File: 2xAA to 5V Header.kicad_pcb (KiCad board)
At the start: 2 copper layers, 30 x 14 mm, 9 parts, among them SW1 SPDT, U1 LTC3426

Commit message: Pin header and corners
Added a two pin header for the output to make attaching leads easier and
cleaned up any 90 degree corners in fills.
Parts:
- added P1: CONN_01X02, Pin_Headers:Pin_Header_Angled_1x02, F.Cu at (176.7, 105.0)
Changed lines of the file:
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@@
 (kicad_pcb (version 4) (host pcbnew 4.0.2-stable)
   (general
-    (links 16)
+    (links 18)
     (no_connects 0)
-    (area 149.924999 95.924999 180.075001 110.075001)
+    (area 147.021999 93.871 190.909334 112.481)
     (thickness 1.6)
     (drawings 17)
     (tracks 76)
     (zones 0)
-    (modules 9)
+    (modules 10)
     (nets 8)
   )
   (page A4)
   (layers
-    (0 F.Cu signal)
+    (0 F.Cu signal hide)
     (31 B.Cu signal)
     (32 B.Adhes user)
@@
     (user_trace_width 0.508)
     (trace_clearance 0.2)
-    (zone_clearance 0.2032)
+    (zone_clearance 0.02032)
     (zone_45_only yes)
     (trace_min 0.1524)
@@
     (add_net /Vout)
   )
+  (module Pin_Headers:Pin_Header_Angled_1x02 (layer F.Cu)
+    (at 176.657 105.029)
+    (descr "Through hole pin header")
+    (tags "pin header")
+    (fp_text reference P1 (at 0 -5.1) (layer F.SilkS)
+      (effects (font (size 1 1) (thickness 0.15)))
+    )
+    (fp_text value CONN_01X02 (at 9.144 -3.556) (layer F.Fab) hide
+      (effects (font (size 1 1) (thickness 0.15)))
+    )
+    (fp_line (start -1.5 -1.75) (end -1.5 4.3) (layer F.CrtYd) (width 0.05))
+    (fp_line (start 10.65 -1.75) (end 10.65 4.3) (layer F.CrtYd) (width 0.05))
+    (fp_line (start -1.5 -1.75) (end 10.65 -1.75) (layer F.CrtYd) (width 0.05))
+    (fp_line (start -1.5 4.3) (end 10.65 4.3) (layer F.CrtYd) (width 0.05))
+    (fp_line (start -1.3 -1.55) (end -1.3 0) (layer F.SilkS) (width 0.15))
+    (fp_line (start 0 -1.55) (end -1.3 -1.55) (layer F.SilkS) (width 0.15))
+    (fp_line (start 4.191 -0.127) (end 10.033 -0.127) (layer F.SilkS) (width 0.15))
+    (fp_line (start 10.033 -0.127) (end 10.033 0.127) (layer F.SilkS) (width 0.15))
+    (fp_line (start 10.033 0.127) (end 4.191 0.127) (layer F.SilkS) (width 0.15))
+    (fp_line (start 4.191 0.127) (end 4.191 0) (layer F.SilkS) (width 0.15))
+    (fp_line (start 4.191 0) (end 10.033 0) (layer F.SilkS) (width 0.15))
+    (fp_line (start 1.524 -0.254) (end 1.143 -0.254) (layer F.SilkS) (width 0.15))
+    (fp_line (start 1.524 0.254) (end 1.143 0.254) (layer F.SilkS) (width 0.15))
+    (fp_line (start 1.524 2.286) (end 1.143 2.286) (layer F.SilkS) (width 0.15))
+    (fp_line (start 1.524 2.794) (end 1.143 2.794) (layer F.SilkS) (width 0.15))
+    (fp_line (start 1.524 -1.27) (end 4.064 -1.27) (layer F.SilkS) (width 0.15))
+    (fp_line (start 1.524 1.27) (end 4.064 1.27) (layer F.SilkS) (width 0.15))
+    (fp_line (start 1.524 1.27) (end 1.524 3.81) (layer F.SilkS) (width 0.15))
+    (fp_line (start 1.524 3.81) (end 4.064 3.81) (layer F.SilkS) (width 0.15))
+    (fp_line (start 4.064 2.286) (end 10.16 2.286) (layer F.SilkS) (width 0.15))
+    (fp_line (start 10.16 2.286) (end 10.16 2.794) (layer F.SilkS) (width 0.15))
+    (fp_line (start 10.16 2.794) (end 4.064 2.794) (layer F.SilkS) (width 0.15))
+    (fp_line (start 4.064 3.81) (end 4.064 1.27) (layer F.SilkS) (width 0.15))
+    (fp_line (start 4.064 1.27) (end 4.064 -1.27) (layer F.SilkS) (width 0.15))
+    (fp_line (start 10.16 0.254) (end 4.064 0.254) (layer F.SilkS) (width 0.15))
+    (fp_line (start 10.16 -0.254) (end 10.16 0.254) (layer F.SilkS) (width 0.15))
+    (fp_line (start 4.064 -0.254) (end 10.16 -0.254) (layer F.SilkS) (width 0.15))
+    (fp_line (start 1.524 1.27) (end 4.064 1.27) (layer F.SilkS) (width 0.15))
+    (fp_line (start 1.524 -1.27) (end 1.524 1.27) (layer F.SilkS) (width 0.15))
+    (pad 1 thru_hole rect (at 0 0) (size 2.032 2.032) (drill 1.016) (layers *.Cu *.Mask F.SilkS)
+      (net 3 /Vout))
+    (pad 2 thru_hole oval (at 0 2.54) (size 2.032 2.032) (drill 1.016) (layers *.Cu *.Mask F.SilkS)
+      (net 1 GND))
+    (model Pin_Headers.3dshapes/Pin_Header_Angled_1x02.wrl
+      (at (xyz 0 -0.05 0))
+      (scale (xyz 1 1 1))
+      (rotate (xyz 0 0 90))
+    )
+  )
   (module .pretty:JS102011SAQN (layer F.Cu)
     (at 153.797 105.537 270)
@@
     )
   )
-  (gr_text - (at 178.816 107.95) (layer F.SilkS)
+  (gr_text - (at 178.816 109.347) (layer F.SilkS)
     (effects (font (size 1.5 1.5) (thickness 0.3)))
   )
-  (gr_text + (at 178.816 104.648) (layer F.SilkS)
+  (gr_text + (at 178.816 102.235) (layer F.SilkS)
     (effects (font (size 1.5 1.5) (thickness 0.3)))
   )
-  (gr_text "OUT\n" (at 177.292 102.108) (layer F.SilkS)
+  (gr_text "OUT\n" (at 172.72 102.997) (layer F.SilkS)
     (effects (font (size 1.5 1.5) (thickness 0.3)))
   )
@@
   (gr_line (start 162 110) (end 162 105) (angle 90) (layer Edge.Cuts) (width 0.15))
   (gr_line (start 150 110) (end 162 110) (angle 90) (layer Edge.Cuts) (width 0.15))
+  (segment (start 174.812 107.6325) (end 176.5935 107.6325) (width 0.5) (layer B.Cu) (net 1))
+  (segment (start 176.5935 107.6325) (end 176.657 107.569) (width 0.5) (layer B.Cu) (net 1))
   (segment (start 155.714 108.204) (end 157.48 108.204) (width 0.5) (layer F.Cu) (net 1))
   (via (at 155.714 108.204) (size 0.6) (drill 0.4) (layers F.Cu B.Cu) (net 1))
@@
   (segment (start 153.797 108.037) (end 155.547 108.037) (width 0.5) (layer F.Cu) (net 1))
   (via (at 174.812 107.6325) (size 0.6) (drill 0.4) (layers F.Cu B.Cu) (net 1))
-  (segment (start 174.812 107.6325) (end 175.3835 108.204) (width 0.5) (layer F.Cu) (net 1))
   (segment (start 173.562 107.6325) (end 174.812 107.6325) (width 0.5) (layer F.Cu) (net 1))
-  (segment (start 175.3835 108.204) (end 176.276 108.204) (width 0.5) (layer F.Cu) (net 1))
   (segment (start 171.4935 99.822) (end 171.4935 104.314) (width 0.5) (layer B.Cu) (net 1))
   (segment (start 171.4935 104.314) (end 174.812 107.6325) (width 0.5) (layer B.Cu) (net 1))
@@
     (polygon
       (pts
-        (xy 162.814 99.822) (xy 164.084 99.822) (xy 169.418 99.822) (xy 169.7228 100.076) (xy 169.7228 101.4476)
-        (xy 168.0972 101.4476) (xy 161.4932 101.4476) (xy 159.258 103.632) (xy 156.21 103.632) (xy 154.686 102.108)
-        (xy 154.686 98.044) (xy 160.02 98.044) (xy 160.02 99.822) (xy 161.417 99.822)
-      )
-    )
-  )
-  (zone (net 1) (net_name GND) (layer F.Cu) (hatch edge 0.508)
-    (connect_pads yes (clearance 0.02032))
-    (min_thickness 0.0254)
-    (fill yes (arc_segments 16) (thermal_gap 0.508) (thermal_bridge_width 0.508))
-    (polygon
-      (pts
-        (xy 175.26 109.474) (xy 177.8 109.474) (xy 177.8 106.934) (xy 175.26 106.934)
+        (xy 159.893 99.822) (xy 169.418 99.822) (xy 169.7228 100.076) (xy 169.7228 101.4476) (xy 161.4932 101.4476)
+        (xy 159.258 103.632) (xy 156.21 103.632) (xy 154.686 102.108) (xy 154.686 98.044) (xy 159.512 98.044)
+        (xy 159.512 98.298) (xy 159.766 98.552) (xy 159.766 99.695) (xy 159.893 99.822)
       )
     )
@@
     (polygon
       (pts
-        (xy 170.5356 98.0948) (xy 170.5356 101.9048) (xy 170.942 102.362) (xy 177.8 102.362) (xy 177.8 106.172)
         (xy 172.466 106.172) (xy 171.958 105.918) (xy 171.958 104.14) (xy 169.926 103.378) (xy 164.7952 103.378)
         (xy 164.7952 101.7016) (xy 170.0276 101.7016) (xy 170.0276 100.0252) (xy 169.5196 99.568) (xy 167.64 99.568)
         (xy 167.132 99.314) (xy 164.338 99.314) (xy 164.338 96.52) (xy 168.91 96.52) (xy 170.434 98.044)
+        (xy 170.5356 98.0948) (xy 170.5356 101.9048) (xy 170.942 102.362) (xy 177.165 102.362) (xy 177.8 102.997)
+        (xy 177.8 106.172) (xy 172.466 106.172)
       )
     )
@@
     (polygon
       (pts
-        (xy 168.402 109.474) (xy 168.402 104.648) (xy 161.544 104.648) (xy 161.544 109.474) (xy 151.892 109.474)
-        (xy 151.892 101.6) (xy 155.702 96.52) (xy 174.244 96.52) (xy 179.578 101.854) (xy 179.578 109.474)
+        (xy 179.578 101.854) (xy 179.578 108.966) (xy 179.07 109.474) (xy 168.91 109.474) (xy 168.402 108.966)
+        (xy 168.402 104.902) (xy 168.148 104.648) (xy 161.798 104.648) (xy 161.544 104.902) (xy 161.544 108.966)
+        (xy 161.036 109.474) (xy 152.4 109.474) (xy 151.892 108.966) (xy 151.892 101.6) (xy 155.702 96.52)
+        (xy 174.244 96.52) (xy 179.578 101.854)
       )
     )
-  )
-  (zone (net 0) (net_name "") (layer F.Mask) (hatch edge 0.508)
-    (connect_pads yes (clearance 0.02032))
-    (min_thickness 0.0254)
-    (fill yes (arc_segments 16) (thermal_gap 0.508) (thermal_bridge_width 0.508))
-    (polygon
-      (pts
-        (xy 177.8 106.934) (xy 175.26 106.934) (xy 175.26 109.474) (xy 177.8 109.474)
-      )
-    )
-  )
-  (zone (net 0) (net_name "") (layer F.Mask) (hatch edge 0.508)
-    (connect_pads yes (clearance 0.02032))
-    (min_thickness 0.0254)
-    (fill yes (arc_segments 16) (thermal_gap 0.508) (thermal_bridge_width 0.508))
-    (polygon
-      (pts
-        (xy 177.8 106.172) (xy 175.26 106.172) (xy 175.26 103.632) (xy 177.8 103.632)
-      )
-    )

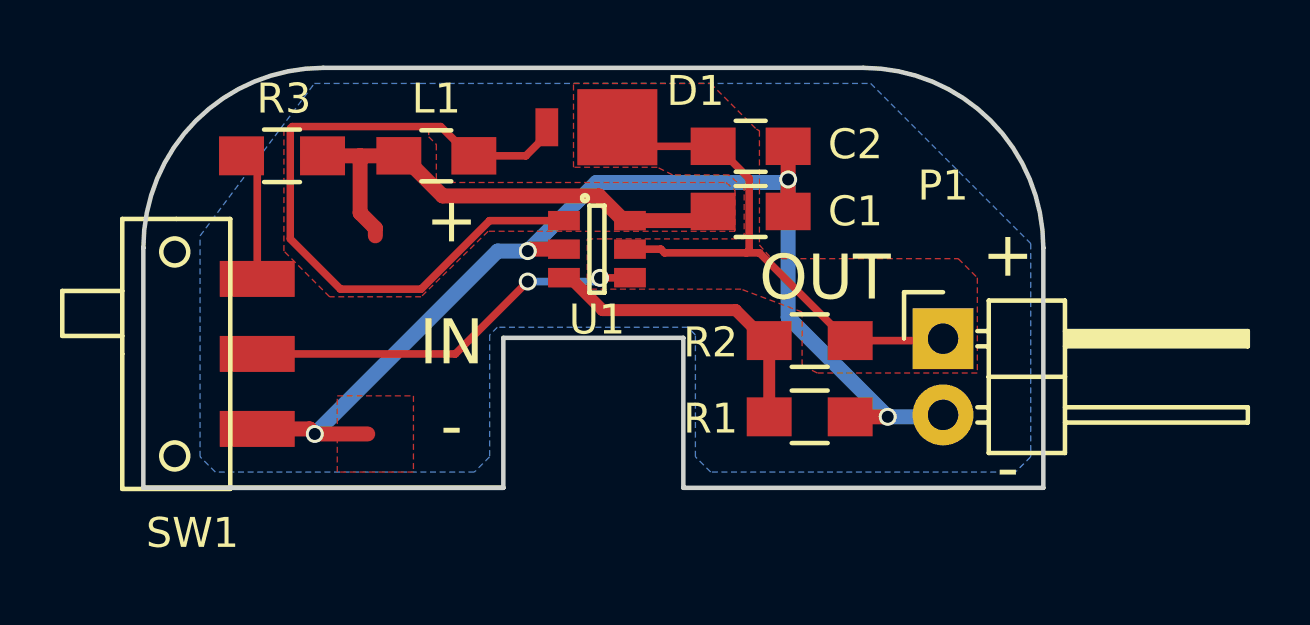
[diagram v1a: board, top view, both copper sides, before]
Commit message: Redo of GND copper fill
Reworked the GND copper fills to cover better and use thermal reliefs.
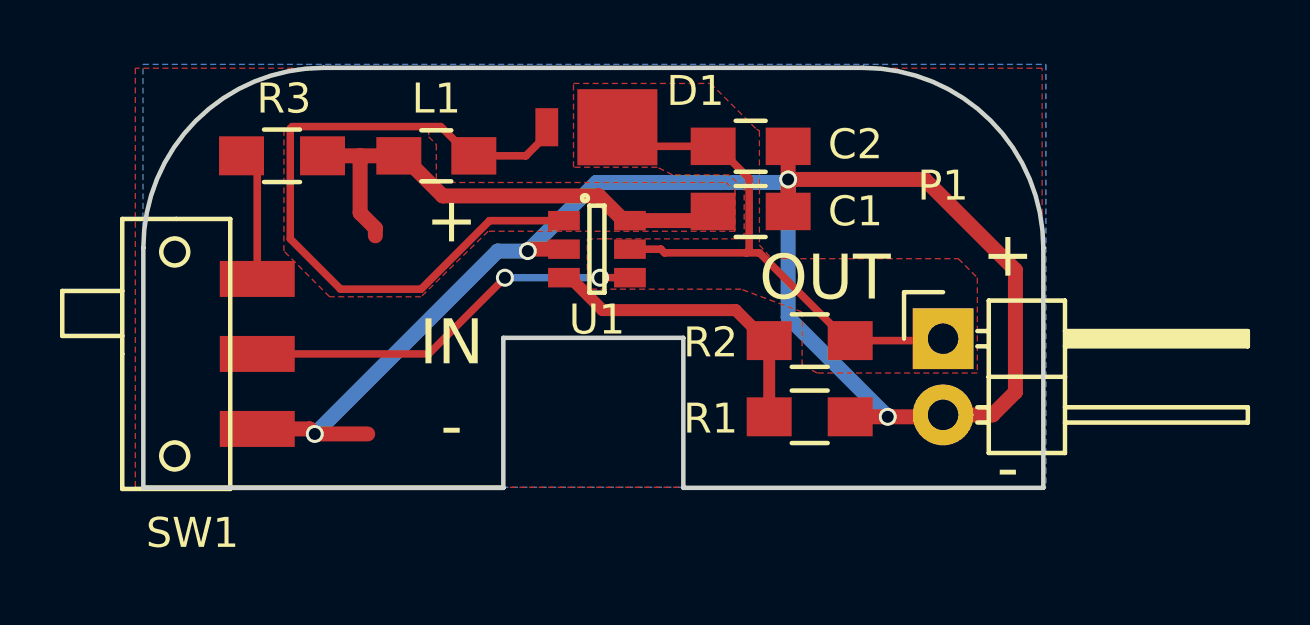
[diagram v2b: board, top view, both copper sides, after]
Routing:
- net GND: track 39.7 -> 55.4 mm
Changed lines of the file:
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@@
     (thickness 1.6)
     (drawings 17)
-    (tracks 76)
+    (tracks 82)
     (zones 0)
     (modules 10)
@@
   (page A4)
   (layers
-    (0 F.Cu signal hide)
+    (0 F.Cu signal)
     (31 B.Cu signal)
     (32 B.Adhes user)
@@
     (user_trace_width 0.508)
     (trace_clearance 0.2)
-    (zone_clearance 0.02032)
+    (zone_clearance 0.1524)
     (zone_45_only yes)
     (trace_min 0.1524)
@@
   (gr_line (start 162 110) (end 162 105) (angle 90) (layer Edge.Cuts) (width 0.15))
   (gr_line (start 150 110) (end 162 110) (angle 90) (layer Edge.Cuts) (width 0.15))
-  (segment (start 174.812 107.6325) (end 176.5935 107.6325) (width 0.5) (layer B.Cu) (net 1))
+  (segment (start 171.4935 99.7204) (end 176.0474 99.7204) (width 0.5) (layer F.Cu) (net 1))
+  (via (at 171.4935 99.7204) (size 0.6) (drill 0.4) (layers F.Cu B.Cu) (net 1))
+  (segment (start 178.308 107.569) (end 176.657 107.569) (width 0.5) (layer F.Cu) (net 1))
+  (segment (start 179.07 106.807) (end 178.308 107.569) (width 0.5) (layer F.Cu) (net 1))
+  (segment (start 179.07 102.743) (end 179.07 106.807) (width 0.5) (layer F.Cu) (net 1))
+  (segment (start 176.0474 99.7204) (end 179.07 102.743) (width 0.5) (layer F.Cu) (net 1))
+  (segment (start 174.812 107.6325) (end 176.5935 107.6325) (width 0.5) (layer F.Cu) (net 1))
+  (segment (start 176.5935 107.6325) (end 176.657 107.569) (width 0.5) (layer F.Cu) (net 1))
   (segment (start 176.5935 107.6325) (end 176.657 107.569) (width 0.5) (layer B.Cu) (net 1))
   (segment (start 155.714 108.204) (end 157.48 108.204) (width 0.5) (layer F.Cu) (net 1))
@@
   (segment (start 171.4935 101.092) (end 171.4935 99.822) (width 0.5) (layer F.Cu) (net 1))
   (segment (start 171.4935 98.6155) (end 171.4935 99.822) (width 0.5) (layer F.Cu) (net 1))
-  (via (at 171.4935 99.7204) (size 0.6) (drill 0.4) (layers F.Cu B.Cu) (net 1))
   (segment (start 164.0205 102.0445) (end 162.8775 102.0445) (width 0.5) (layer F.Cu) (net 1))
   (segment (start 162.8775 102.0445) (end 162.814 102.108) (width 0.5) (layer F.Cu) (net 1))
@@
   (segment (start 170.862 105.0925) (end 170.762 105.0925) (width 0.4) (layer F.Cu) (net 5))
   (segment (start 170.762 105.0925) (end 169.746 104.0765) (width 0.4) (layer F.Cu) (net 5))
-  (segment (start 165.222482 103.001518) (end 166.213482 103.001518) (width 0.254) (layer F.Cu) (net 6))
-  (via (at 162.814 103.124) (size 0.6) (drill 0.4) (layers F.Cu B.Cu) (net 6))
-  (segment (start 160.401 105.537) (end 162.814 103.124) (width 0.254) (layer F.Cu) (net 6))
-  (segment (start 153.797 105.537) (end 160.401 105.537) (width 0.254) (layer F.Cu) (net 6))
-  (via (at 165.222482 103.001518) (size 0.6) (drill 0.4) (layers F.Cu B.Cu) (net 6))
-  (segment (start 165.1 103.124) (end 165.222482 103.001518) (width 0.254) (layer B.Cu) (net 6))
-  (segment (start 162.814 103.124) (end 165.1 103.124) (width 0.254) (layer B.Cu) (net 6))
+  (segment (start 153.797 105.537) (end 159.512 105.537) (width 0.25) (layer F.Cu) (net 6))
+  (segment (start 165.2295 102.9945) (end 166.2205 102.9945) (width 0.25) (layer F.Cu) (net 6))
+  (segment (start 165.227 102.997) (end 165.2295 102.9945) (width 0.25) (layer F.Cu) (net 6))
+  (via (at 165.227 102.997) (size 0.6) (drill 0.4) (layers F.Cu B.Cu) (net 6))
+  (segment (start 162.052 102.997) (end 165.227 102.997) (width 0.25) (layer B.Cu) (net 6))
+  (via (at 162.052 102.997) (size 0.6) (drill 0.4) (layers F.Cu B.Cu) (net 6))
+  (segment (start 159.512 105.537) (end 162.052 102.997) (width 0.25) (layer F.Cu) (net 6))
   (segment (start 166.213482 103.001518) (end 166.2205 102.9945) (width 0.25) (layer F.Cu) (net 6))
   (segment (start 166.1595 102.9335) (end 166.2205 102.9945) (width 0.25) (layer F.Cu) (net 6))
@@
   (segment (start 153.797 99.4575) (end 153.2725 98.933) (width 0.254) (layer F.Cu) (net 7))
   (zone (net 2) (net_name /Vin) (layer F.Cu) (hatch edge 0.508)
+    (priority 1)
     (connect_pads yes (clearance 0.1524))
     (min_thickness 0.1524)
@@
   )
   (zone (net 3) (net_name /Vout) (layer F.Cu) (hatch edge 0.508)
+    (priority 1)
     (connect_pads yes (clearance 0.2032))
     (min_thickness 0.1524)
@@
     (polygon
       (pts
-        (xy 172.466 106.172) (xy 171.958 105.918) (xy 171.958 104.14) (xy 169.926 103.378) (xy 164.7952 103.378)
-        (xy 164.7952 101.7016) (xy 170.0276 101.7016) (xy 170.0276 100.0252) (xy 169.5196 99.568) (xy 167.64 99.568)
-        (xy 167.132 99.314) (xy 164.338 99.314) (xy 164.338 96.52) (xy 168.91 96.52) (xy 170.434 98.044)
-        (xy 170.5356 98.0948) (xy 170.5356 101.9048) (xy 170.942 102.362) (xy 177.165 102.362) (xy 177.8 102.997)
-        (xy 177.8 106.172) (xy 172.466 106.172)
-      )
-    )
-  )
-  (zone (net 1) (net_name GND) (layer B.Cu) (hatch edge 0.508)
-    (connect_pads yes (clearance 0.02032))
-    (min_thickness 0.0254)
-    (fill yes (arc_segments 16) (thermal_gap 0.508) (thermal_bridge_width 0.508))
-    (polygon
-      (pts
-        (xy 179.578 101.854) (xy 179.578 108.966) (xy 179.07 109.474) (xy 168.91 109.474) (xy 168.402 108.966)
-        (xy 168.402 104.902) (xy 168.148 104.648) (xy 161.798 104.648) (xy 161.544 104.902) (xy 161.544 108.966)
-        (xy 161.036 109.474) (xy 152.4 109.474) (xy 151.892 108.966) (xy 151.892 101.6) (xy 155.702 96.52)
-        (xy 174.244 96.52) (xy 179.578 101.854)
+        (xy 170.434 98.044) (xy 170.5356 98.0948) (xy 170.5356 101.9048) (xy 170.942 102.362) (xy 177.165 102.362)
+        (xy 177.8 102.997) (xy 177.8 106.172) (xy 172.466 106.172) (xy 171.958 105.918) (xy 171.958 104.14)
+        (xy 169.926 103.378) (xy 164.7952 103.378) (xy 164.7952 101.7016) (xy 170.0276 101.7016) (xy 170.0276 100.0252)
+        (xy 169.5196 99.568) (xy 167.64 99.568) (xy 167.132 99.314) (xy 164.338 99.314) (xy 164.338 96.52)
+        (xy 168.91 96.52) (xy 170.434 98.044)
       )
     )
@@
   )
   (zone (net 1) (net_name GND) (layer F.Cu) (hatch edge 0.508)
-    (connect_pads yes (clearance 0.02032))
+    (connect_pads (clearance 0.1524))
     (min_thickness 0.0254)
     (fill yes (arc_segments 16) (thermal_gap 0.508) (thermal_bridge_width 0.508))
     (polygon
       (pts
-        (xy 156.464 109.474) (xy 156.464 106.934) (xy 159.004 106.934) (xy 159.004 109.474)
+        (xy 179.959 109.855) (xy 179.959 96.012) (xy 149.733 96.012) (xy 149.733 109.982) (xy 179.959 109.982)
+        (xy 179.959 109.855)
       )
     )
+  )
+  (zone (net 1) (net_name GND) (layer B.Cu) (hatch edge 0.508)
+    (connect_pads (clearance 0.254))
+    (min_thickness 0.0254)
+    (fill yes (arc_segments 16) (thermal_gap 0.508) (thermal_bridge_width 0.508))
+    (polygon
+      (pts
+        (xy 180.086 109.982) (xy 149.987 109.982) (xy 149.987 95.885) (xy 180.086 95.885) (xy 180.086 109.982)
+      )
+    )
